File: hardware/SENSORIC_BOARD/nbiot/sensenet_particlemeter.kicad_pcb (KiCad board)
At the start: 2 copper layers, 63.6 x 72.3 mm, 80 parts, among them J1 CONN_01X01, J11 CONN_01X01, J13 BARREL_JACK, J17 CONN_01X01, J18 CONN_01X01, J19 CONN_01X01, J2 CONN_01X01, J20 CONN_01X01, J21 CONN_01X01, J3 CONN_01X01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

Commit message: Zaklad nove verze je hotovy, ted jdu udelat vetsi zmeny v napajeni a layoutu, priprava na shield atd.
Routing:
- net GND: track 262.0 -> 269.2 mm, vias 29 -> 30
- net +3V3: track 212.4 -> 211.1 mm
- net PM_SDI: track 15.6 -> 16.6 mm
- net PM_SDO: track 15.9 -> 16.7 mm
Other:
- net class Default: trace_width 0.5 -> 0.15

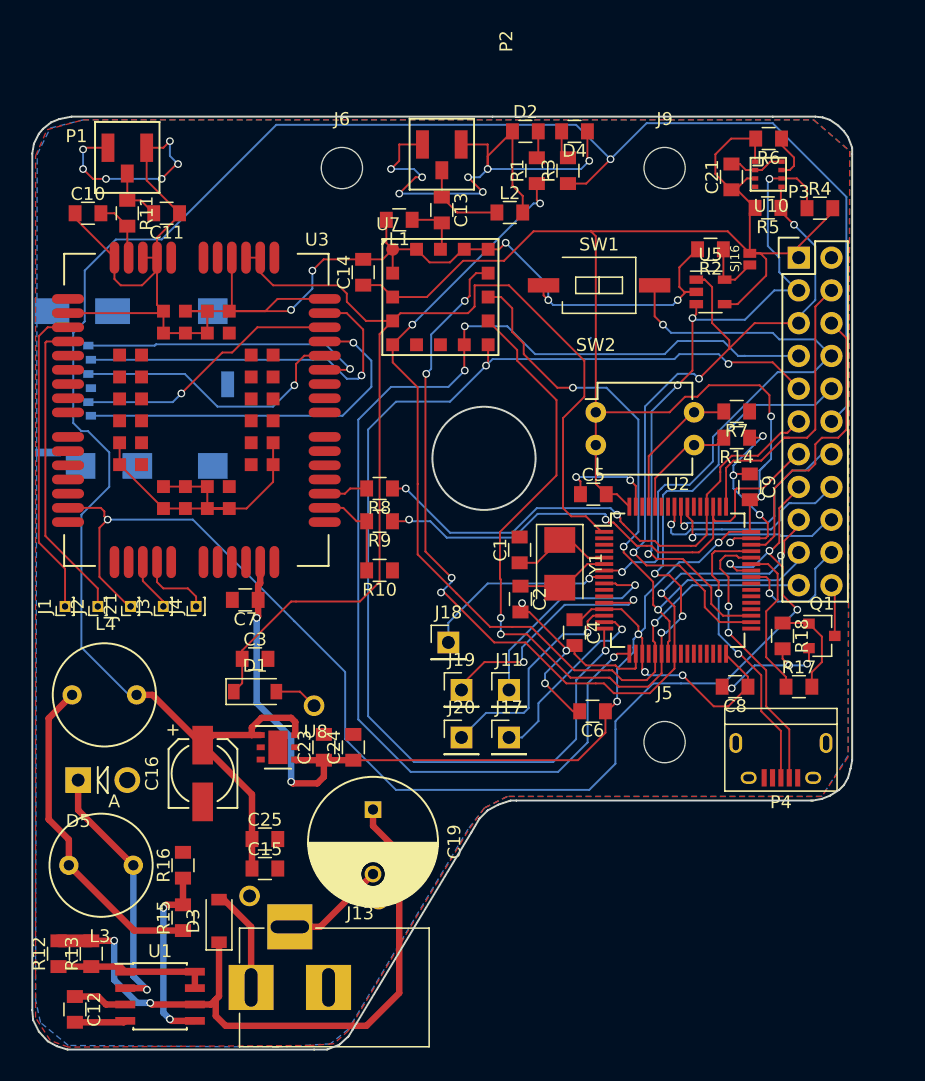
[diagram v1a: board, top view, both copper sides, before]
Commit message: Novy rozmer desky, zmena napajeni z LDO na step down, pridany 1000uF na 5V
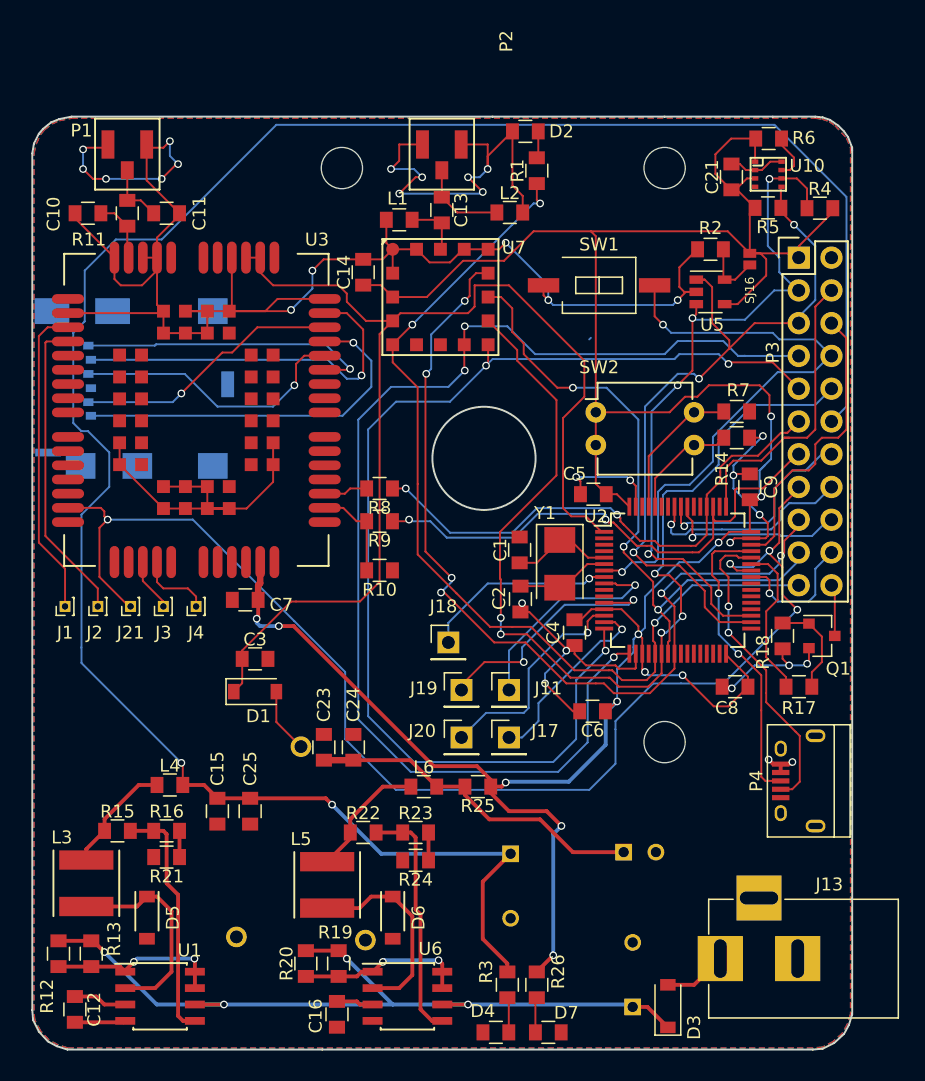
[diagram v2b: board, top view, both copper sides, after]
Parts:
- removed U8: LD39050, SNPM:DFN-6-1EP_3x3mm_Pitch0.95mm
- added C17: 1000u, SNPM:C_Radial_D10_L16_P5_bottom, F.Cu at (169.2, 110.6)
- added C18: 470uF, SNPM:C_Radial_D6.3_L11.2_P2.5_bottom, F.Cu at (177.9, 110.5)
- added D6: 1N5819, Diodes_SMD:SOD-123, F.Cu at (160.0, 115.6)
- added D7: LED, SNPM:SMD_0805, F.Cu at (172.1, 124.5)
- added L5: 41uH, Inductors:Inductor_Taiyo-Yuden_NR-50xx, F.Cu at (154.9, 113.0)
- added L6: 1uH, SNPM:SMD_0805, F.Cu at (162.4, 105.4)
- added R19: 0R33, SNPM:SMD_0805, F.Cu at (155.8, 119.1)
- added R20: tbd, SNPM:SMD_0805, F.Cu at (153.3, 119.1)
- added R21: tbd, SNPM:SMD_0805, F.Cu at (142.5, 110.9)
- added R22: 18k, SNPM:SMD_0805, F.Cu at (157.7, 109.0)
- added R23: 11k, SNPM:SMD_0805, F.Cu at (161.8, 109.0)
- added R24: tbd, SNPM:SMD_0805, F.Cu at (161.8, 111.1)
- added R25: 0R1, SNPM:SMD_0805, F.Cu at (166.6, 105.4)
- added R26: 5k6, SNPM:SMD_0805, F.Cu at (171.2, 120.8)
- added U6: MC33063, Housings_SOIC:SOIC-8_3.9x4.9mm_Pitch1.27mm, F.Cu at (161.2, 121.7)
- C12: value 470pF -> 510pF
- C16: value 100uF -> 352pF; footprint Capacitors_SMD:c_elec_5x5.3 -> SNPM:SMD_0805
- C19: footprint Capacitors_ThroughHole:C_Radial_D10_L16_P5 -> SNPM:C_Radial_D10_L16_P5_bottom
- D5: footprint Diodes_ThroughHole:Diode_DO-41_SOD81_Vertical_AnodeUp -> Diodes_SMD:SOD-123
- L3: value 220uH -> 39uH; footprint Inductors_NEOSID:Neosid_Inductor_Sd8 -> Inductors:Inductor_Taiyo-Yuden_NR-50xx
- L4: footprint Inductors_NEOSID:Neosid_Inductor_Sd8 -> SNPM:SMD_0805
- R12: value 0R47 -> 0R33
- R13: value 0R47 -> tbd
- R15: value R -> 27k
- R16: value R -> 9.1k
- moved D4 70.1 mm to (168.0, 124.5), turned to 0 degrees
- moved R3 63.3 mm to (168.9, 120.8), turned to 270 degrees
- moved J13 36.4 mm to (185.4, 118.7)
- moved D3 35.4 mm to (181.4, 122.4)
- moved C19 25.3 mm to (178.6, 122.5), turned to 90 degrees
- moved C16 21.4 mm to (155.7, 123.1)
- moved D5 11.9 mm to (141.0, 115.6), turned to 270 degrees
- moved L4 8.64 mm to (142.7, 105.3)
- moved R15 8.43 mm to (138.7, 108.8), turned to 0 degrees
- moved C15 5.77 mm to (146.4, 107.3), turned to 270 degrees
- moved BT1 3.33 mm to (152.9, 107.1)
- moved R16 2.95 mm to (142.5, 108.8), turned to 0 degrees
- moved C25 2.44 mm to (149.0, 107.3), turned to 270 degrees
- moved P4 2.07 mm to (191.5, 105.0), turned to 90 degrees
- moved L3 1.81 mm to (136.3, 112.9), turned to 90 degrees
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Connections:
- net Net-(C19-Pad1) renamed +9V
- C16 pad 1: +5V -> Net-(C16-Pad1)
- C23 pad 1: +3V3 -> Net-(C18-Pad1)
- C24 pad 1: +3V3 -> Net-(C18-Pad1)
- R16 pad 2: GND -> Net-(R16-Pad2)
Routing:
- net Net-(C18-Pad1): track 0.00 -> 26.6 mm
- net Net-(R22-Pad2): track 0.00 -> 18.8 mm
- net Net-(L3-Pad2): track 25.6 -> 8.92 mm
- net GND: track 269.2 -> 253.3 mm, vias 30 -> 31
- net Net-(D6-Pad1): track 0.00 -> 15.7 mm
- net Net-(R19-Pad1): track 0.00 -> 13.1 mm, vias 0 -> 2
- net +3V3: track 211.1 -> 223.8 mm, vias 9 -> 12
- net +5V: track 157.2 -> 168.3 mm, vias 1 -> 2
- net +9V: track 52.7 -> 62.7 mm, vias 2 -> 4
- net Net-(L5-Pad2): track 0.00 -> 9.78 mm
- net Net-(R15-Pad2): track 14.5 -> 18.8 mm, vias 2 -> 0
- net Net-(D5-Pad1): track 20.2 -> 16.2 mm, vias 1 -> 0
- net Net-(C16-Pad1): track 0.00 -> 2.86 mm
- net Net-(D3-Pad2): track 8.06 -> 5.26 mm
- net Net-(D7-Pad2): track 0.00 -> 2.73 mm
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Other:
- outline, holes or cut-outs redrawn
- net class Default: trace_width 0.15 -> 0.3
- rule via_min_size: 0.3 -> 0.4

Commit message: zonglovani zase s gitem
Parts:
- moved J18 0.99 mm to (165.3, 94.2)
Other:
- net class Default: trace_width 0.3 -> 0.15
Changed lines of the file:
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@@
     (links 242)
     (no_connects 0)
-    (area 132.004999 53.391999 195.718501 125.868501)
+    (area 131.498999 45.56 212.32 128.768477)
     (thickness 1.6)
     (drawings 34)
-    (tracks 1195)
+    (tracks 1197)
     (zones 0)
     (modules 94)
@@
   )
   (setup
-    (last_trace_width 0.3)
+    (last_trace_width 0.15)
     (trace_clearance 0.15)
     (zone_clearance 0.2)
@@
   (net_class Default "This is the default net class."
     (clearance 0.15)
-    (trace_width 0.3)
+    (trace_width 0.15)
     (via_dia 0.6)
     (via_drill 0.4)
@@
   )
   (module SNPM:Pin_Header_Straight_1x01_Pitch2.54mm (layer F.Cu)
-    (at 164.338 94.234)
+    (at 165.3286 94.234)
     (descr "Through hole straight pin header, 1x01, 2.54mm pitch, single row")
     (tags "Through hole pin header THT 1x01 2.54mm single row")
@@
   (via (at 177.8 93.218) (size 0.6) (drill 0.4) (layers F.Cu B.Cu) (net 45))
   (segment (start 177.24 92.658) (end 177.8 93.218) (width 0.15) (layer F.Cu) (net 45))
+  (segment (start 165.3286 94.234) (end 165.3286 91.7194) (width 0.15) (layer B.Cu) (net 46))
+  (segment (start 165.3286 91.7194) (end 167.386 89.662) (width 0.15) (layer B.Cu) (net 46))
+  (segment (start 167.386 89.662) (end 167.9702 89.662) (width 0.15) (layer B.Cu) (net 46))
   (segment (start 176.418 89.158) (end 175.383 89.158) (width 0.15) (layer F.Cu) (net 46))
-  (segment (start 164.338 92.71) (end 164.338 94.234) (width 0.15) (layer B.Cu) (net 46))
-  (segment (start 167.386 89.662) (end 164.338 92.71) (width 0.15) (layer B.Cu) (net 46))
-  (segment (start 174.879 89.662) (end 167.386 89.662) (width 0.15) (layer B.Cu) (net 46))
+  (segment (start 174.879 89.662) (end 167.9702 89.662) (width 0.15) (layer B.Cu) (net 46))
+  (segment (start 167.9702 89.662) (end 167.386 89.662) (width 0.15) (layer B.Cu) (net 46))
   (segment (start 175.26 89.281) (end 174.879 89.662) (width 0.15) (layer B.Cu) (net 46))
   (via (at 175.26 89.281) (size 0.6) (drill 0.4) (layers F.Cu B.Cu) (net 46))

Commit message: objednavam prototypy
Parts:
- removed J9: CONN_01X01, SNPM:MountingHole_3.2mm_M3_DIN965
- added D10: LED, SNPM:SMD_0805, F.Cu at (172.3, 122.8)
- added D8: LED, SNPM:SMD_0805, F.Cu at (166.2, 122.8)
- added D9: LED, SNPM:SMD_0805, F.Cu at (169.2, 122.8)
- added R27: R, SNPM:SMD_0805, F.Cu at (171.7, 115.7)
- added R28: R, SNPM:SMD_0805, F.Cu at (173.9, 115.7)
- added R29: R, SNPM:SMD_0805, F.Cu at (176.1, 115.7)
- added SW3: SW_DPST, SNPM:edge_switch, F.Cu at (179.1, 123.8)
- P3: value CONN_02X11 -> CONN_02X12; footprint Pin_Headers:Pin_Header_Straight_2x11 -> Pin_Headers:Pin_Header_Straight_2x12
- SW1: value SW_Push -> SW_DPST; footprint SNPM:SW_DIP_x1_W8.61mm_Slide_SMD_LowProfile -> SNPM:edge_switch
- SW2: value SW_DIP_x02 -> SW_DIP_x03; footprint Housings_DIP:DIP-4_W7.62mm -> Housings_DIP:DIP-6_W7.62mm
- moved R3 23.9 mm to (145.6, 115.4)
- moved R26 21.3 mm to (150.6, 115.4)
- moved D7 20.0 mm to (152.1, 123.9)
- moved D4 19.9 mm to (148.1, 123.9), turned to 180 degrees
- moved SW1 11.5 mm to (176.3, 55.1)
- moved SW2 11.4 mm to (172.8, 65.3)
- moved D3 6.54 mm to (181.5, 115.9), turned to 270 degrees
- moved R7 6.01 mm to (181.1, 78.5)
- moved R14 5.88 mm to (181.1, 76.5)
- moved C19 3.77 mm to (180.8, 119.4), turned to 180 degrees
- moved P3 2.55 mm to (191.5, 61.8)
- moved R4 2.53 mm to (193.2, 58.0), turned to 90 degrees
- moved R5 1.79 mm to (187.5, 61.2)
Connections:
- P3 pad 1: +3V3 -> USART_debug_tx
- P3 pad 10: gps_standby -> reset
- P3 pad 11: Rx -> UART_GPS_TX
- P3 pad 12: +5V -> gps_standby
- P3 pad 13: Tx -> Rx
- P3 pad 14: PM_SDO -> +5V
- P3 pad 15: WIRELESS_reset -> Tx
- P3 pad 16: PM_SDI -> PM_SDO
- P3 pad 17: gps_pulses -> WIRELESS_reset
- P3 pad 18: PM_SCK -> PM_SDI
- P3 pad 19: gps_reset -> gps_pulses
- P3 pad 2: GND -> USART_debug_rx
- P3 pad 20: PM_SS -> PM_SCK
- P3 pad 21: gps_fix -> gps_reset
- P3 pad 22: Net-(P3-Pad22) -> PM_SS
- P3 pad 3: i2c_sda -> +3V3
- P3 pad 4: SWD_CLK -> GND
- P3 pad 5: i2c_scl -> i2c_sda
- P3 pad 6: SWD_DIO -> SWD_CLK
- P3 pad 7: UART_GPS_RX -> i2c_scl
- P3 pad 8: reset -> SWD_DIO
- P3 pad 9: UART_GPS_TX -> UART_GPS_RX
- Q1 pad 3: Net-(P3-Pad22) -> Net-(P3-Pad24)
- SW2 pad 3: BOOT_0 -> debug_on_off
- SW2 pad 4: BOOT_signal -> GND
- U2 pad 2: (no net) -> NETLIGHT
- U2 pad 25: (no net) -> Net-(R27-Pad1)
- U2 pad 27: (no net) -> Net-(R28-Pad1)
- U2 pad 28: (no net) -> Net-(R29-Pad1)
- U2 pad 29: (no net) -> Net-(SW3-Pad1)
- U2 pad 3: (no net) -> RI
- U2 pad 58: (no net) -> USART_debug_tx
- U2 pad 59: (no net) -> USART_debug_rx
- U2 pad 62: (no net) -> debug_on_off
- U3 pad 18: (no net) -> NETLIGHT
- U3 pad 34: (no net) -> RI
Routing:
- net NETLIGHT: track 0.00 -> 49.2 mm, vias 0 -> 2
- net RI: track 0.00 -> 41.8 mm, vias 0 -> 2
- net Net-(SW3-Pad1): track 0.00 -> 38.9 mm
- net USART_debug_rx: track 0.00 -> 32.5 mm
- net Net-(R29-Pad1): track 0.00 -> 32.0 mm
- net Net-(R28-Pad1): track 0.00 -> 30.4 mm
- net Net-(R27-Pad1): track 0.00 -> 30.0 mm
- net USART_debug_tx: track 0.00 -> 26.1 mm
- net debug_on_off: track 0.00 -> 16.0 mm
- net i2c_scl: track 58.4 -> 70.7 mm, vias 3 -> 5
- net reset: track 46.2 -> 56.7 mm, vias 2 -> 4
- net BOOT_0: track 8.83 -> 18.2 mm
- net BOOT_signal: track 11.2 -> 20.0 mm
- net Net-(D8-Pad2): track 0.00 -> 8.37 mm
- net GND: track 253.3 -> 261.4 mm, vias 31 -> 33
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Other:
- net class Default: trace_width 0.15 -> 0.5

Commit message: pred debugem noveho hardwaru
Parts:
- removed P4: USB_B, Connectors:USB_Micro-B
- added ?: , koksovna:drawing, F.Cu at (163.7, 82.1)
- added R30: 0R1, SNPM:SMD_0805, F.Cu at (148.1, 111.1)
- added U8: usb_femalee, Connectors:USB_Micro-B, F.Cu at (192.4, 105.7)
- moved J6 0.08 mm to (156.1, 57.5)
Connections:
- C15 pad 1: +5V -> Net-(C15-Pad1)
- C17 pad 1: +5V -> Net-(C15-Pad1)
- C25 pad 1: +5V -> Net-(C15-Pad1)
- L4 pad 2: +5V -> Net-(C15-Pad1)
- U2 pad 45: PA11-USB-DP -> PA12-USB-DP
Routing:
- net Net-(C15-Pad1): track 0.00 -> 35.7 mm, vias 0 -> 1
- net +5V: track 167.3 -> 142.3 mm, vias 2 -> 1
- net PA12-USB-DP: track 0.00 -> 24.7 mm, vias 0 -> 2
- net PA11-USB-DP: track 23.7 -> 0.00 mm, vias 2 -> 0
- net WIRELESS_reset: track 101.6 -> 104.9 mm, vias 4 -> 5
- net PA11-USB-DM: track 24.0 -> 22.5 mm
- net GND: track 261.4 -> 262.3 mm, vias 33 -> 31
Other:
- net class Default: trace_width 0.5 -> 0.15

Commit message: pred displayem
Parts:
- removed ?: , koksovna:drawing
- removed BT1: Battery_Cell, SNPM:BAT-CR2032_bottom
- removed C1, C2: 4.3p, SNPM:SMD_0805
- removed C24: 220n, SNPM:SMD_0805
- removed C3: C, SNPM:SMD_0805
- removed J17, J20: CONN_01X01, SNPM:Pin_Header_Straight_1x01_Pitch2.54mm
- removed R25, R30: 0R1, SNPM:SMD_0805
- removed Y1: 8MHz, Crystals:Crystal_SMD_5032-2pin_5.0x3.2mm
- added D11: SM2T3V3A, SNPM:D_SOD-123, F.Cu at (136.2, 112.2)
- added L7: FBMH1608HL601-T, Resistors_SMD:R_0603, F.Cu at (161.8, 113.9)
- added L8: FBMH1608HL601-T, Resistors_SMD:R_0603, F.Cu at (139.0, 113.7)
- C15: value 1u -> 1000u; footprint SNPM:SMD_0805 -> SNPM:C_Radial_D10_L16_P5_bottom
- D1: value D_Schottky -> PTVS3V3S1UR,115; footprint SNPM:D_SOD-123 -> SNPM:SMD_0805
- D10, D2, D8, D9: footprint SNPM:SMD_0805 -> SNPM:SMD_0805_bottom
- D4: value LED -> red LED; footprint SNPM:SMD_0805 -> SNPM:SMD_0805_bottom
- D5, D6: footprint Diodes_SMD:SOD-123 -> SNPM:D_SOD-123
- D7: value LED -> green LED; footprint SNPM:SMD_0805 -> SNPM:SMD_0805_bottom
- L3, L5: footprint Inductors:Inductor_Taiyo-Yuden_NR-50xx -> SNPM:Inductor_Taiyo-Yuden_NR-50xx
- L4, L6: value 1uH -> FBMH1608HL601-T; footprint SNPM:SMD_0805 -> Resistors_SMD:R_0603
- P3: footprint Pin_Headers:Pin_Header_Straight_2x12 -> SNPM:Pin_Header_Straight_2x12
- Q1: footprint TO_SOT_Packages_SMD:SOT-23 -> SNPM:SOT-23
- R16: value 9.1k -> 10k
- R22: value 18k -> 8k2
- R23: value 11k -> 5k6
- R26: value 5k6 -> 1k
- R3: value 5k6 -> 8k2
- SW1, SW3: footprint SNPM:edge_switch -> SNPM:edge_switch_bot
- SW2: footprint Housings_DIP:DIP-6_W7.62mm -> SNPM:DIP-6_W7.62mm_bot
- U1: footprint Housings_SOIC:SOIC-8_3.9x4.9mm_Pitch1.27mm -> SNPM:SOIC-8_3.9x4.9mm_Pitch1.27mm
- moved SW1 46.3 mm to (193.5, 98.0), turned to 270 degrees
- moved R12 45.8 mm to (179.9, 118.4)
- moved R13 45.3 mm to (182.0, 118.4)
- moved C12 43.4 mm to (177.7, 113.0), turned to 90 degrees
- moved C18 39.4 mm to (139.1, 117.1), turned to 270 degrees
- moved L3 37.7 mm to (172.7, 122.8), turned to 180 degrees
- moved D5 36.7 mm to (177.6, 117.9)
- moved J5 34.6 mm to (146.6, 100.8)
- moved U1 31.0 mm to (172.1, 114.3), turned to 180 degrees
- moved R15 30.6 mm to (166.9, 120.6), turned to 90 degrees
- moved J2 28.8 mm to (135.3, 62.7)
- moved J1 28.8 mm to (133.2, 62.7)
- moved L6 28.5 mm to (140.1, 123.1)
- moved L4 28.2 mm to (164.5, 123.2)
- moved R16 25.6 mm to (166.9, 116.7), turned to 90 degrees
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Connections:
- C15 pad 1: Net-(C15-Pad1) -> +5V
- C17 pad 1: Net-(C15-Pad1) -> Net-(C17-Pad1)
- C23 pad 1: Net-(C18-Pad1) -> +3V3
- C25 pad 1: Net-(C15-Pad1) -> +5V
- D1 pad 1: batt -> +5V
- D1 pad 2: Net-(BT1-Pad1) -> GND
- L4 pad 1: Net-(L3-Pad2) -> Net-(C17-Pad1)
- L4 pad 2: Net-(C15-Pad1) -> Net-(L3-Pad2)
- L6 pad 1: Net-(L5-Pad2) -> Net-(C18-Pad1)
- L6 pad 2: Net-(C18-Pad1) -> Net-(L5-Pad2)
- P3 pad 1: USART_debug_tx -> i2c_sda
- P3 pad 10: reset -> WIRELESS_reset
- P3 pad 11: UART_GPS_TX -> NMOS
- P3 pad 12: gps_standby -> +5V
- P3 pad 13: Rx -> USART_debug_rx
- P3 pad 14: +5V -> USART_debug_tx
- P3 pad 15: Tx -> PM_SDI
- P3 pad 17: WIRELESS_reset -> PM_SCK
- P3 pad 18: PM_SDI -> PM_SS
- P3 pad 19: gps_pulses -> Rx
- P3 pad 2: USART_debug_rx -> +3V3
- P3 pad 20: PM_SCK -> Tx
- P3 pad 21: gps_reset -> SWD_CLK
- P3 pad 22: PM_SS -> GND
- P3 pad 23: gps_fix -> SWD_DIO
- P3 pad 24: Net-(P3-Pad24) -> reset
- P3 pad 3: +3V3 -> i2c_scl
- P3 pad 4: GND -> gps_pulses
- P3 pad 5: i2c_sda -> gps_reset
- P3 pad 6: SWD_CLK -> gps_standby
- P3 pad 7: i2c_scl -> UART_GPS_TX
- P3 pad 8: SWD_DIO -> UART_GPS_RX
- P3 pad 9: UART_GPS_RX -> gps_fix
- Q1 pad 3: Net-(P3-Pad24) -> NMOS
- R14 pad 2: BOOT_0 -> BOOT_signal
- R7 pad 2: BOOT_signal -> BOOT_0
- SW2 pad 1: +3V3 -> BOOT_0
- SW2 pad 2: +3V3 -> BOOT_signal
- SW2 pad 3: debug_on_off -> GND
- SW2 pad 4: GND -> debug_on_off
- SW2 pad 5: BOOT_0 -> +3V3
- SW2 pad 6: BOOT_signal -> +3V3
- U2 pad 1: batt -> (no net)
- U2 pad 10: (no net) -> gps_pulses
- U2 pad 11: (no net) -> gps_reset
- U2 pad 14: Net-(J20-Pad1) -> gps_standby
- U2 pad 15: Net-(J17-Pad1) -> gps_fix
- U2 pad 2: NETLIGHT -> RI
- U2 pad 21: gps_fix -> (no net)
- U2 pad 22: gps_standby -> (no net)
- U2 pad 23: gps_reset -> (no net)
- U2 pad 24: gps_pulses -> (no net)
- U2 pad 3: RI -> NETLIGHT
- U2 pad 41: PM_SS -> (no net)
- U2 pad 42: WIRELESS_reset -> (no net)
- U2 pad 5: Net-(C1-Pad1) -> (no net)
- U2 pad 53: (no net) -> WIRELESS_reset
- U2 pad 54: (no net) -> PM_SS
- U2 pad 6: Net-(C2-Pad1) -> (no net)
- U7 pad 14: batt -> (no net)
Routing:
- net GND: track 262.3 -> 153.9 mm, vias 31 -> 46
- net batt: track 81.1 -> 1.10 mm, vias 2 -> 0
- net +5V: track 142.3 -> 80.9 mm, vias 1 -> 2
- net Net-(C15-Pad1): track 35.7 -> 0.00 mm, vias 1 -> 0
- net UART_GPS_TX: track 90.6 -> 61.5 mm, vias 3 -> 2
- net Net-(R29-Pad1): track 32.0 -> 3.40 mm
- net UART_GPS_RX: track 97.0 -> 68.7 mm, vias 3 -> 2
- net Net-(R28-Pad1): track 30.4 -> 3.27 mm
- net Net-(R27-Pad1): track 30.0 -> 3.73 mm
- net +3V3: track 230.9 -> 254.9 mm, vias 13 -> 8
- net reset: track 56.7 -> 34.4 mm, vias 4 -> 1
- net debug_on_off: track 16.0 -> 37.6 mm
- net NMOS: track 0.00 -> 20.1 mm, vias 0 -> 1
- net Net-(D10-Pad2): track 7.04 -> 26.5 mm, vias 0 -> 1
- net Net-(D9-Pad2): track 7.03 -> 25.6 mm, vias 0 -> 1
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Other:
- board size 63.6 x 72.3 mm -> 63.6 x 72.4 mm
- net class Default: trace_width 0.15 -> 0.5
- rule pad_to_mask_clearance: 0.2 -> 0.15
